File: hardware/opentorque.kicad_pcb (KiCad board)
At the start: 4 copper layers, 60 x 60 mm, 79 parts, among them Q1 30N06_C5807887, Q2 30N06_C5807887, Q3 30N06_C5807887, Q4 30N06_C5807887, Q5 30N06_C5807887, Q6 30N06_C5807887, SW1 TS-1088-AR02016, U1 RP2040, U10 AS5600-ASOT, U11 AMS1117-3.3_C347222, U2 W25Q128JVSIQTR, U3 SLM2003ECA-DG, U4 INA180A3IDBVR, U5 SLM2003ECA-DG, U6 INA180A3IDBVR, U7 SLM2003ECA-DG, U8 INA180A3IDBVR, U9 UMW78M12, X1 X322512MSB4SI

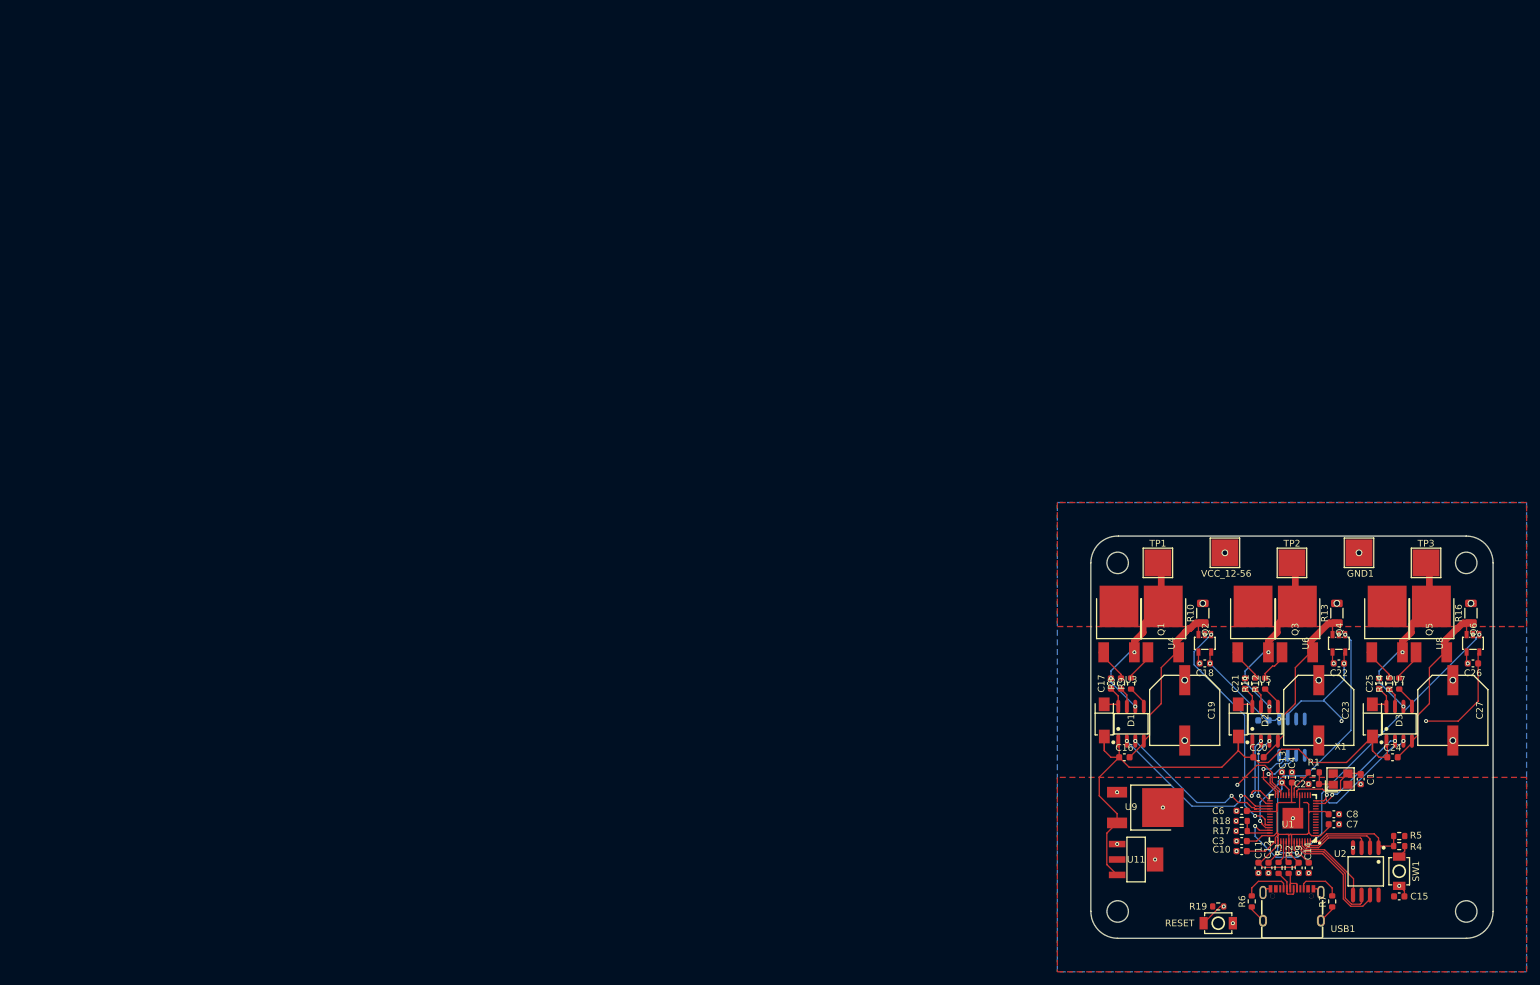
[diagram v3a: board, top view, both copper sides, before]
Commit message: Add LEDs and expand copper pours
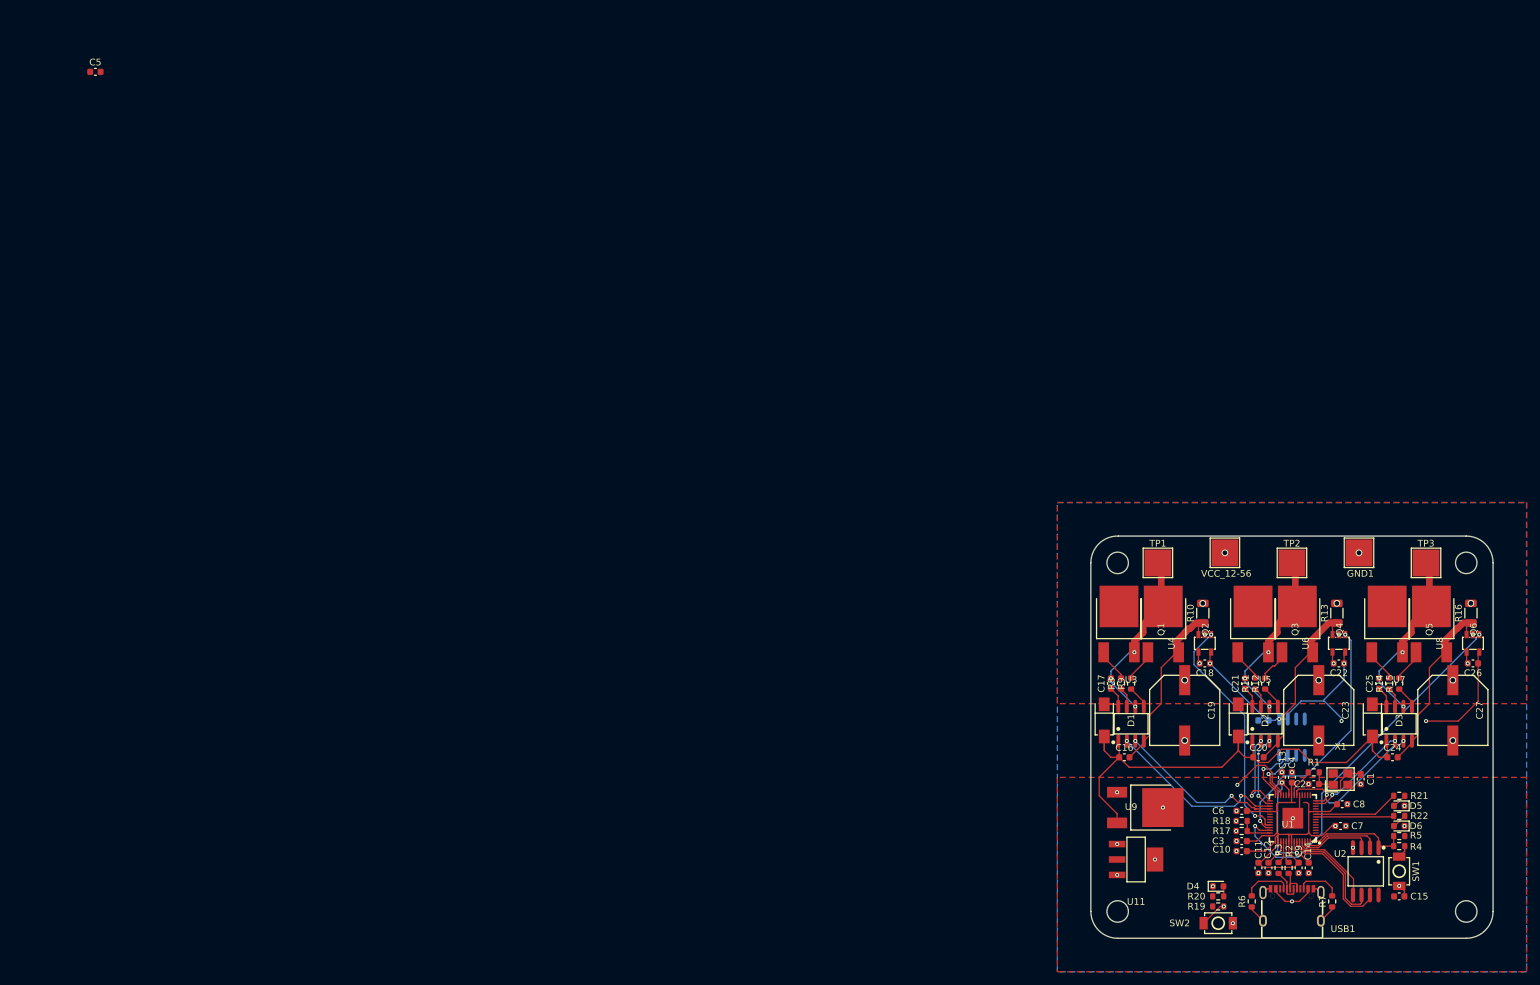
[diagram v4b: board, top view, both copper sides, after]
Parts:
- added C5: 100n, Capacitor_SMD:C_0603_1608Metric, F.Cu at (1.50, 0.76)
- added D4: LED, LED_SMD:LED_0603_1608Metric, F.Cu at (169.0, 122.2)
- added D5: LED, LED_SMD:LED_0603_1608Metric, F.Cu at (196.0, 110.2)
- added D6: LED, LED_SMD:LED_0603_1608Metric, F.Cu at (196.0, 113.2)
- added R20: 68R, Resistor_SMD:R_0603_1608Metric, F.Cu at (169.0, 123.8)
- added R21: 68R, Resistor_SMD:R_0603_1608Metric, F.Cu at (196.0, 108.8)
- added R22: 68R, Resistor_SMD:R_0603_1608Metric, F.Cu at (196.0, 111.8)
- moved C8 1.95 mm to (187.5, 110.0)
- moved C7 1.03 mm to (187.2, 113.2)
- renumbered RESET to SW2
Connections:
- net Net-(U1-RUN) renamed /rp2040/RUN
- U11 pad 3: +12V -> /rp2040/VBUS
- USB1 pad 11: unconnected-(USB1-VBUS-Pad11) -> /rp2040/VBUS
- USB1 pad 2: unconnected-(USB1-VBUS-Pad2) -> /rp2040/VBUS
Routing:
- net VCC: track 0.00 -> 60.2 mm
- net /rp2040/VBUS: track 0.00 -> 36.8 mm, vias 0 -> 2
- net /rp2040/GPIO7: track 0.00 -> 12.8 mm
- net /rp2040/GPIO6: track 0.00 -> 11.7 mm
- net +12V: track 89.9 -> 80.9 mm
- net Net-(D6-A): track 0.00 -> 2.23 mm
- net Net-(D5-A): track 0.00 -> 2.23 mm
- net +3V3: track 160.2 -> 162.1 mm, vias 6 -> 7
- net Net-(D4-A): track 0.00 -> 1.52 mm
- net GND: vias 33 -> 36
- added copper zone on In2.Cu, net +3V3

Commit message: Improve trace widths and decoupling
This should improve system stability
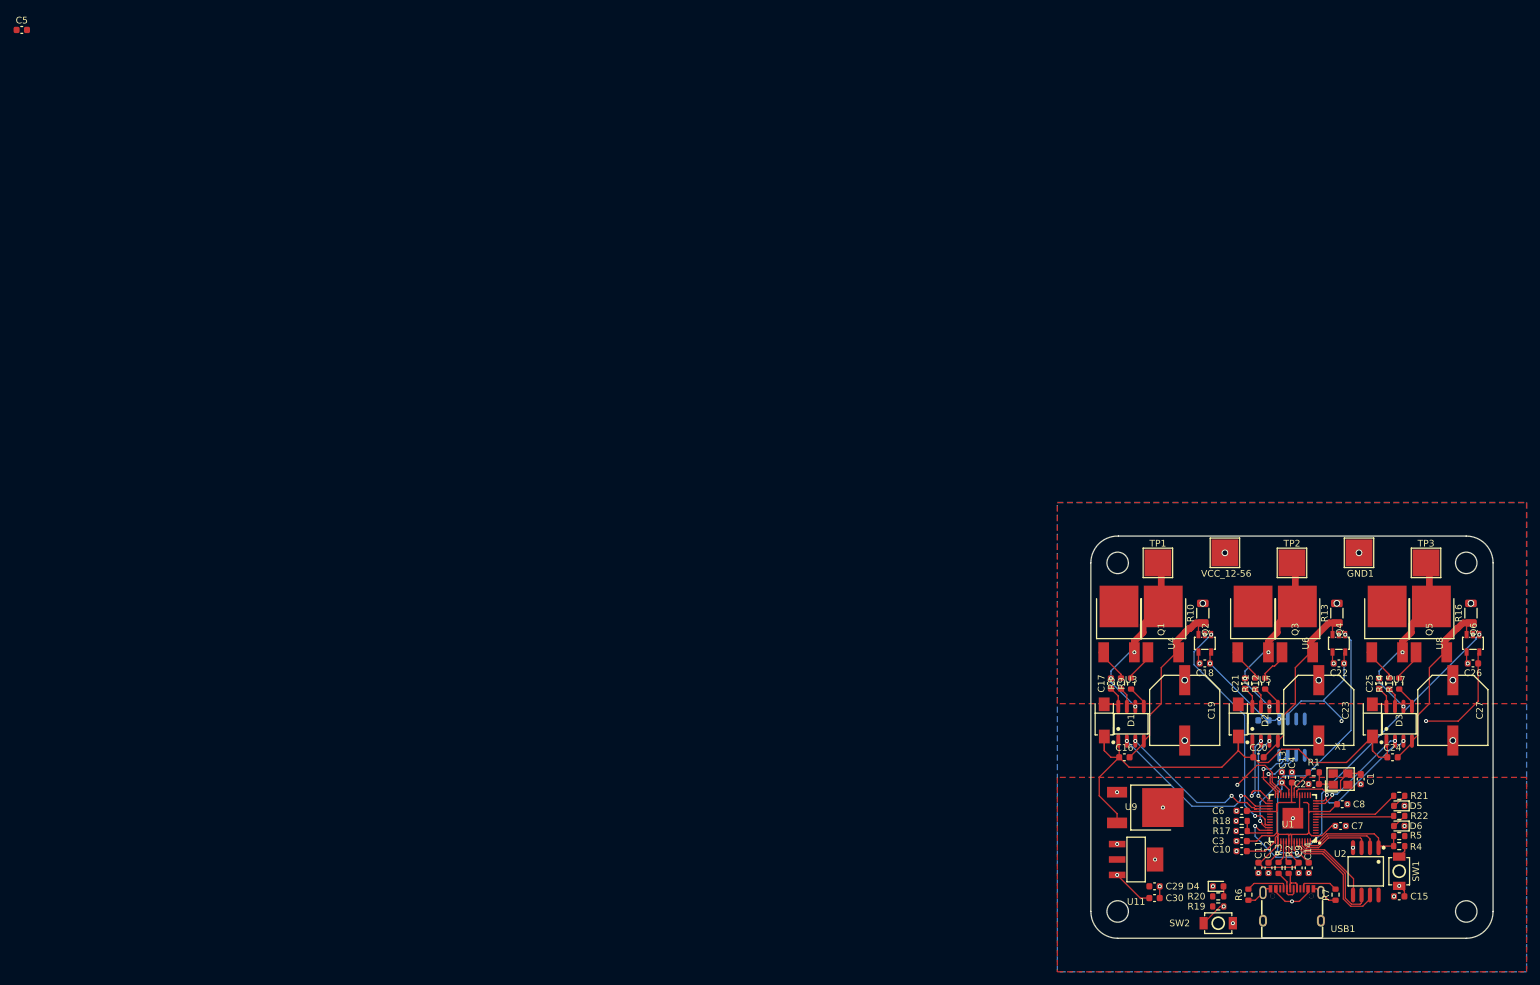
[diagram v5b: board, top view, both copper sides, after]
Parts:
- added C29: 100n, Capacitor_SMD:C_0603_1608Metric, F.Cu at (159.5, 122.2)
- added C30: 100n, Capacitor_SMD:C_0603_1608Metric, F.Cu at (159.5, 124.0)
- moved C5 12.6 mm to (-9.47, -5.50)
- moved R6 1.12 mm to (173.5, 123.5)
- moved R7 1.12 mm to (186.5, 123.5)
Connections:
- X1 pad 2: unconnected-(X1-GND-Pad2) -> GND
- X1 pad 4: unconnected-(X1-GND-Pad4) -> GND
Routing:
- net /rp2040/VBUS: track 36.8 -> 43.0 mm
- net GND: track 19.3 -> 20.8 mm, vias 36 -> 37
- net Net-(USB1-CC2): track 6.76 -> 5.83 mm
- net Net-(USB1-CC1): track 7.27 -> 6.35 mm
- net +3V3: vias 7 -> 8
